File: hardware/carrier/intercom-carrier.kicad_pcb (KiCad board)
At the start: 2 copper layers, 90 x 48 mm, 36 parts, among them J1 P4 pins 1-20, J2 Button 1 (JST-XH), J3 Button 2 (JST-XH), J4 Button 3 (JST-XH), J5 Button 4 (JST-XH), J6 Spare GPIO2/3, J7 P4 pins 21-40, Q1 BC547, Q2 BC547, Q3 BC547, Q4 BC547

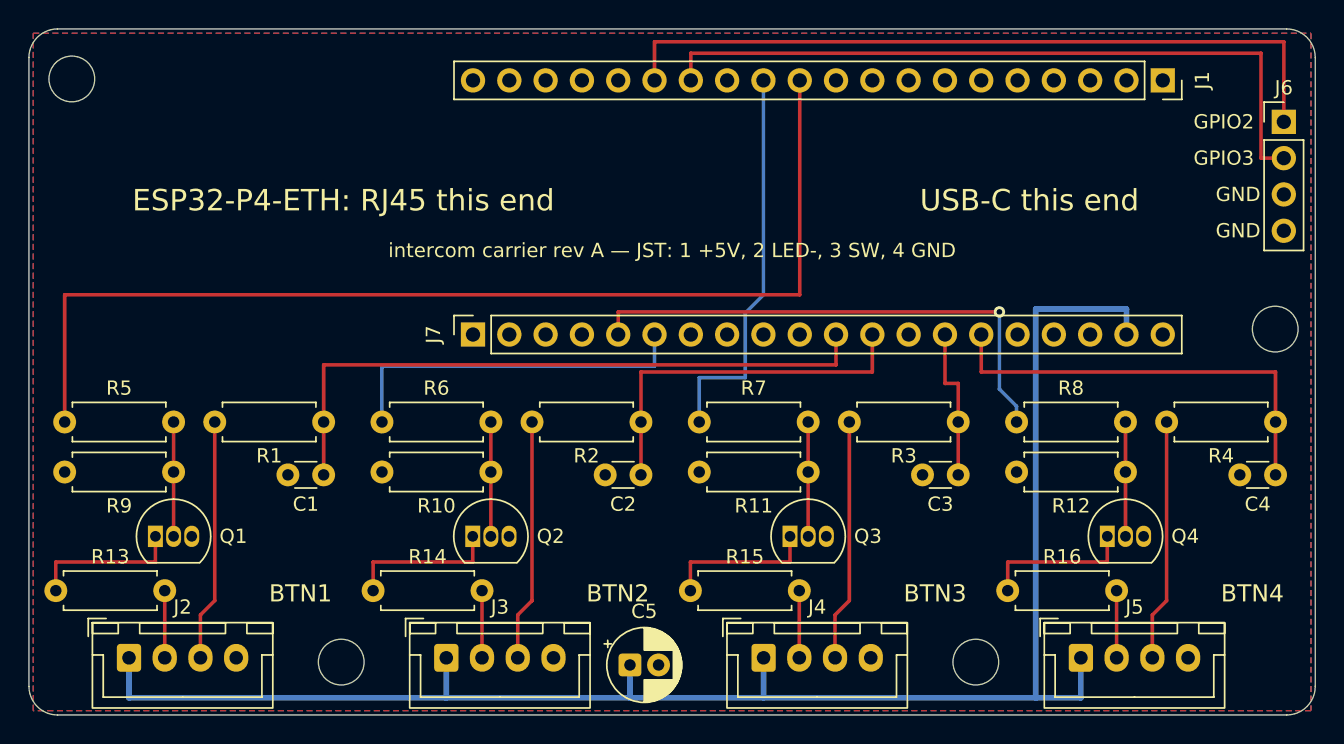
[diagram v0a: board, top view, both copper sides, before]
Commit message: carrier rev B: off switch connector J8 on 3V3_EN
J8 (JST-XH 2-pin, 1 = 3V3_EN / P4 pin 37, 2 = GND) with C6 100 nF across it,
in the bottom-right corner next to the button JSTs. J5 moved 1.1 mm left to
make room; its tracks are re-routed. 3V3_EN runs on B.Cu from J7.17.
Mounting holes and J6 are unchanged, so the enclosure is too.
ERC clean, DRC 0 errors / 0 unconnected. carrier/export/ is still rev A.

Co-Authored-By: Claude Opus 5.5 <noreply@anthropic.com>
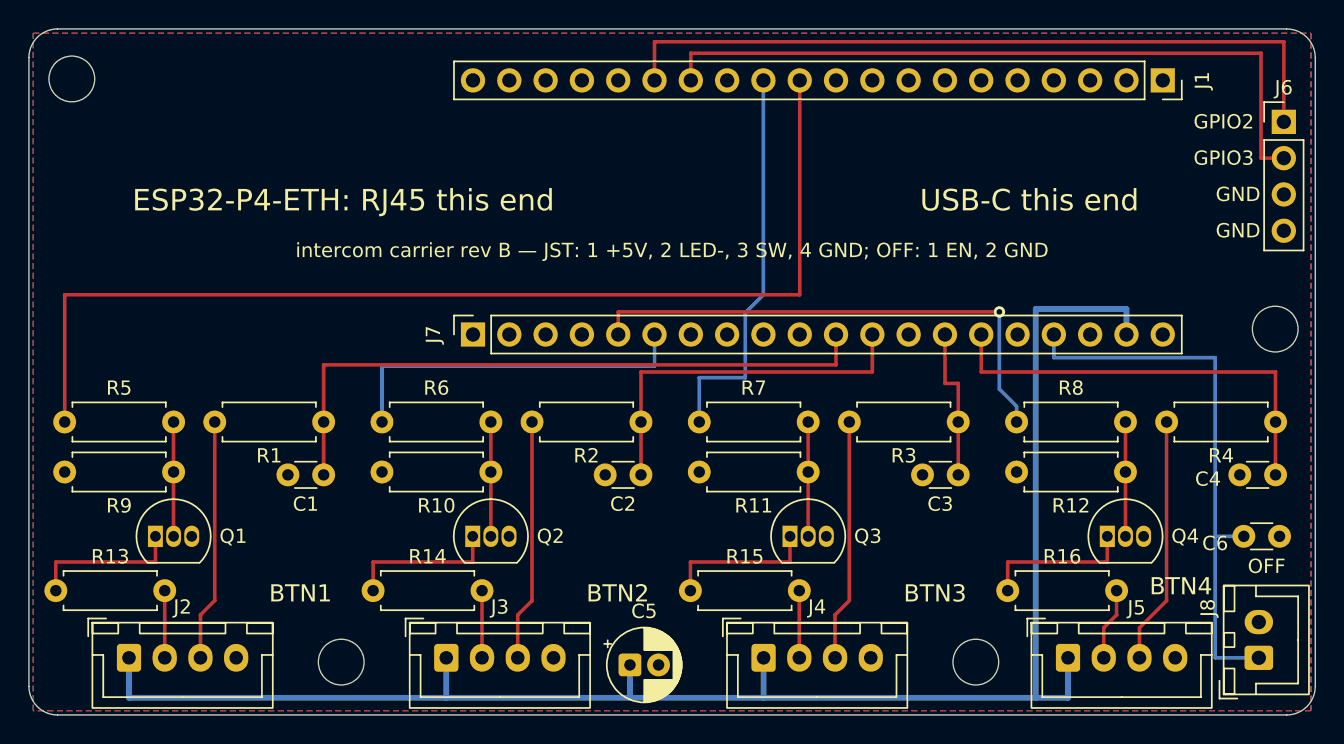
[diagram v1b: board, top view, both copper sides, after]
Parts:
- added C6: 100nF, Capacitor_THT:C_Disc_D3.0mm_W1.6mm_P2.50mm, F.Cu at (185.0, 135.5)
- added J8: Off switch (JST-XH), Connector_JST:JST_XH_B2B-XH-A_1x02_P2.50mm_Vertical, F.Cu at (186.1, 144.0)
- moved J5 0.90 mm to (172.7, 144.0)
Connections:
- J7 pad 17: unconnected-(J7-Pin_17-Pad17) -> /3V3_EN
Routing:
- net /3V3_EN: track 0.00 -> 39.0 mm
- net +5V: track 115.4 -> 114.5 mm
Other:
- board text added: "OFF"
- board text added: "intercom carrier rev B — JST: 1 +5V, 2 LED-, 3 SW, 4 GND; OFF: 1 EN, 2 GND"
- board text removed: "intercom carrier rev A — JST: 1 +5V, 2 LED-, 3 SW, 4 GND"
